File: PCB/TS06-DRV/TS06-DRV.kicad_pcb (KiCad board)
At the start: 2 copper layers, 100 x 70 mm, 38 parts, among them J1 TS06_JST_PH_S6B-PH-K-S_Back, U1 TS06_Arduino_Nano_Back, U11 TS06_DIP-8_Back, U12 TS06_DIP-8_Back, U13 TS06_PinHeader_1x05_Back, U14 TS06_R78E_SIP3_Back

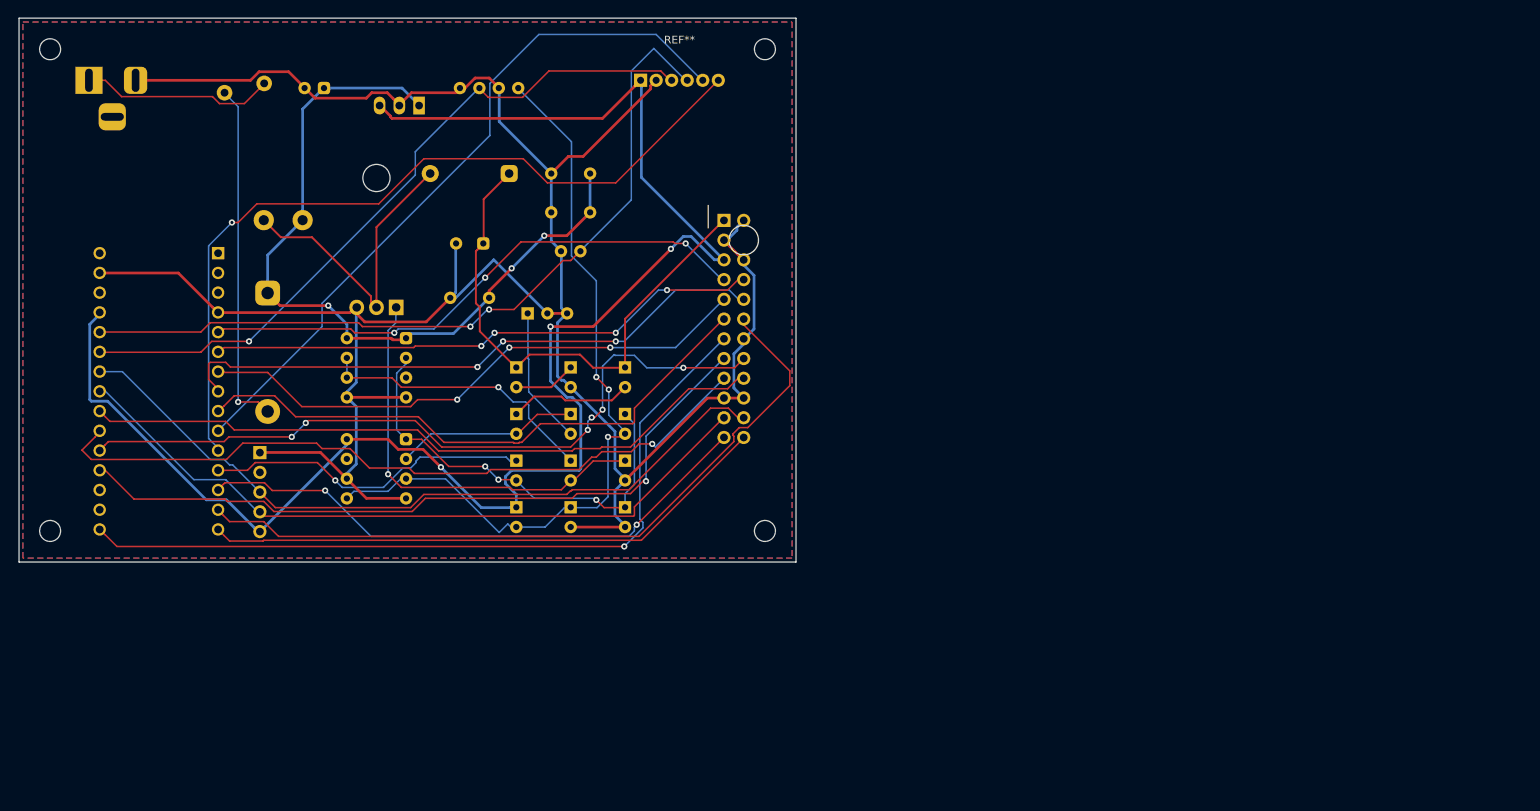
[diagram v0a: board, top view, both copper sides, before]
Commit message: TS06-DRV: routed, no vias, clean in KiCad 10's DRC
The route converged in negotiated routing: round 16, 0 nets sharing, 0 unrouted. A polish
pass then re-routed each net alone. The route is saved in tools/mkpcb_drv_routes.json, so the
board regenerates exactly.
- 1067 segments, 0 vias. Every strip pin and standoff lines up with TS06-DISP (check_mate()
  == []).
- checkcopper --hv is clean, audit.py is clean, and B.check finds 0 problems.
- KiCad 10 DRC: 0 errors and 0 unconnected. Four warnings remain:
  - the Nano's USB outline is proud of the edge, by design;
  - the stock silkscreen of VT21 and XS1 is clipped at their pads.

Fixes on the way:
- The router: an end snapped sideways onto another track now jogs to it instead of tilting
  the whole last run. A 13 mm GND run 0.1 mm out of true had clipped a U15 pad.
- The port-A bus and the LED ribbon are 0.24 mm wide. At their 0.45 mm pitch that leaves
  0.21 mm, not a rounding error under 0.2.
- Three GND pads whose back pour was a sliver fenced by tracks keep out of the pours. KiCad
  had reported starved thermals; the slivers now go as islands.
- References keep off every printed outline, the electrolytic's hatching included.
- audit.py measures a rotated text as rotated.
- plot() takes None as the default colour.

Co-Authored-By: Claude Opus 5.5 <noreply@anthropic.com>
Claude-Session: https://claude.ai/code/session_01WoV3gyAFgmtuk6W6Dr4bdA
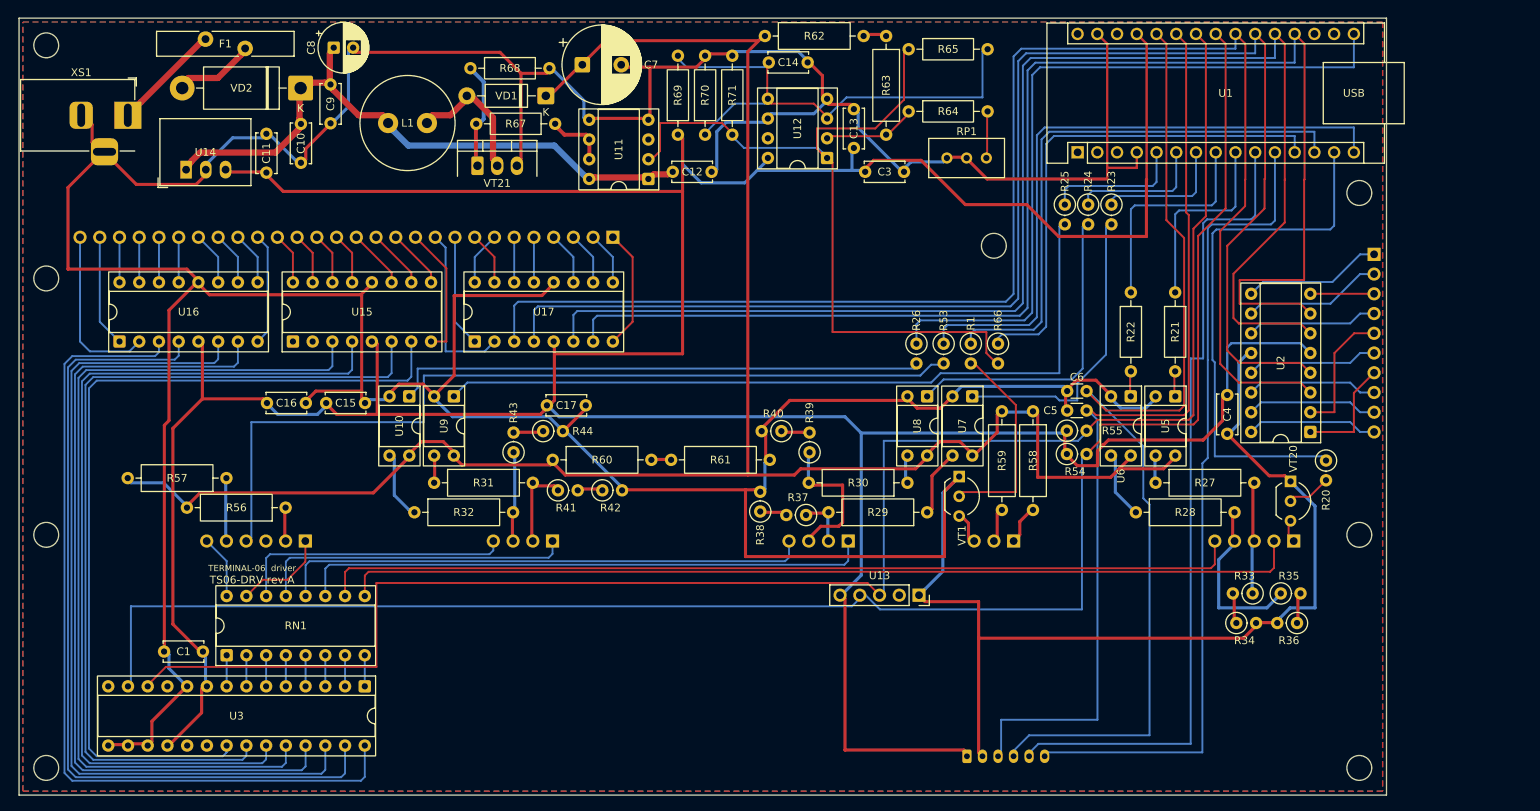
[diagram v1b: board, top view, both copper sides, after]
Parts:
- removed ? (x4): , MountingHole_2.7mm
- removed XJ2: TS06_PinHeader_2x12, TS06:TS06_PinHeader_2x12
- added C1: 100n, TS06:TS06_C_Disc_P5.00mm_R180, F.Cu at (23.7, 81.5)
- added C11: 10u, TS06:TS06_C_Disc_P5.00mm_R90, F.Cu at (31.8, 19.9)
- added C13: 100n, TS06:TS06_C_Disc_P5.00mm_R90, F.Cu at (107.4, 16.7)
- added C15: 100n, TS06:TS06_C_Disc_P5.00mm, F.Cu at (39.5, 49.5)
- added C16: 100n, TS06:TS06_C_Disc_P5.00mm, F.Cu at (31.9, 49.5)
- added C17: 100n, TS06:TS06_C_Disc_P5.00mm, F.Cu at (67.9, 49.8)
- added C3: 10u, TS06:TS06_C_Disc_P5.00mm, F.Cu at (108.9, 19.8)
- added C4: 100n, TS06:TS06_C_Disc_P5.00mm_R270, F.Cu at (155.5, 48.5)
- added H1: TS06_MountingHole_M3, TS06:TS06_MountingHole_M3, F.Cu at (172.5, 66.5)
- added H2: TS06_MountingHole_M3, TS06:TS06_MountingHole_M3, F.Cu at (3.50, 66.5)
- added H3: TS06_MountingHole_M3, TS06:TS06_MountingHole_M3, F.Cu at (125.5, 29.3)
- added H4: TS06_MountingHole_M3, TS06:TS06_MountingHole_M3, F.Cu at (3.50, 33.5)
- added H5: TS06_MountingHole_M3, TS06:TS06_MountingHole_M3, F.Cu at (3.50, 96.5)
- added H6: TS06_MountingHole_M3, TS06:TS06_MountingHole_M3, F.Cu at (172.5, 96.5)
- added H7: TS06_MountingHole_M3, TS06:TS06_MountingHole_M3, F.Cu at (3.50, 3.50)
- added H8: TS06_MountingHole_M3, TS06:TS06_MountingHole_M3, F.Cu at (172.5, 22.5)
- added R1: 10k, TS06:TS06_R_Axial_DIN0207_P2.54mm_Vertical_R270, F.Cu at (122.5, 41.9)
- added R20: 470R, TS06:TS06_R_Axial_DIN0207_P2.54mm_Vertical_R270, F.Cu at (168.2, 56.9)
- added R21: 470R, TS06:TS06_R_Axial_DIN0207_P10.16mm_R270, F.Cu at (148.8, 35.3)
- added R22: 470R, TS06:TS06_R_Axial_DIN0207_P10.16mm_R270, F.Cu at (143.1, 35.3)
- added R23: 470R, TS06:TS06_R_Axial_DIN0207_P2.54mm_Vertical_R270, F.Cu at (140.6, 24.0)
- added R24: 470R, TS06:TS06_R_Axial_DIN0207_P2.54mm_Vertical_R270, F.Cu at (137.6, 24.0)
- added R25: 470R, TS06:TS06_R_Axial_DIN0207_P2.54mm_Vertical_R270, F.Cu at (134.6, 24.0)
- added R26: 470R, TS06:TS06_R_Axial_DIN0207_P2.54mm_Vertical_R270, F.Cu at (115.5, 41.9)
- added R27: 6k8 TBC, TS06:TS06_R_Axial_DIN0309_P12.70mm, F.Cu at (146.3, 59.8)
- added R28: 6k8 TBC, TS06:TS06_R_Axial_DIN0309_P12.70mm, F.Cu at (143.7, 63.6)
- added R29: 6k8 TBC, TS06:TS06_R_Axial_DIN0309_P12.70mm_R180, F.Cu at (116.9, 63.6)
- added R30: 6k8 TBC, TS06:TS06_R_Axial_DIN0309_P12.70mm_R180, F.Cu at (114.3, 59.8)
- added R31: 12k, TS06:TS06_R_Axial_DIN0309_P12.70mm, F.Cu at (53.4, 59.8)
- added R32: 12k, TS06:TS06_R_Axial_DIN0309_P12.70mm, F.Cu at (50.9, 63.6)
- added R33: 510k DNP, TS06:TS06_R_Axial_DIN0207_P2.54mm_Vertical_R180, F.Cu at (158.8, 74.0)
- added R34: 510k DNP, TS06:TS06_R_Axial_DIN0207_P2.54mm_Vertical, F.Cu at (156.7, 77.8)
- added R35: 510k DNP, TS06:TS06_R_Axial_DIN0207_P2.54mm_Vertical, F.Cu at (162.4, 74.0)
- added R36: 510k DNP, TS06:TS06_R_Axial_DIN0207_P2.54mm_Vertical_R180, F.Cu at (164.5, 77.8)
- added R37: 510k DNP, TS06:TS06_R_Axial_DIN0207_P2.54mm_Vertical_R180, F.Cu at (101.3, 64.0)
- added R38: 510k DNP, TS06:TS06_R_Axial_DIN0207_P2.54mm_Vertical_R90, F.Cu at (95.4, 63.5)
- added R39: 510k DNP, TS06:TS06_R_Axial_DIN0207_P2.54mm_Vertical_R90, F.Cu at (101.7, 55.9)
- added R40: 510k DNP, TS06:TS06_R_Axial_DIN0207_P2.54mm_Vertical_R180, F.Cu at (98.1, 53.2)
- added R41: 510k DNP, TS06:TS06_R_Axial_DIN0207_P2.54mm_Vertical, F.Cu at (69.4, 60.8)
- added R42: 510k DNP, TS06:TS06_R_Axial_DIN0207_P2.54mm_Vertical, F.Cu at (75.1, 60.8)
- added R43: 510k DNP, TS06:TS06_R_Axial_DIN0207_P2.54mm_Vertical_R90, F.Cu at (63.6, 55.9)
- added R44: 510k DNP, TS06:TS06_R_Axial_DIN0207_P2.54mm_Vertical, F.Cu at (67.5, 53.2)
- added R53: 220R, TS06:TS06_R_Axial_DIN0207_P2.54mm_Vertical_R270, F.Cu at (119.0, 41.9)
- added R54: 4k7, TS06:TS06_R_Axial_DIN0207_P2.54mm_Vertical, F.Cu at (134.9, 56.1)
- added R55: 4k7, TS06:TS06_R_Axial_DIN0207_P2.54mm_Vertical, F.Cu at (134.9, 53.1)
- added R56: 8k2, TS06:TS06_R_Axial_DIN0309_P12.70mm_R180, F.Cu at (34.3, 63.0)
- added R57: 8k2, TS06:TS06_R_Axial_DIN0309_P12.70mm_R180, F.Cu at (26.7, 59.2)
- added R58: 220k, TS06:TS06_R_Axial_DIN0309_P12.70mm_R270, F.Cu at (130.5, 50.6)
- added R59: 220k, TS06:TS06_R_Axial_DIN0309_P12.70mm_R270, F.Cu at (126.5, 50.6)
- added RN1: 8x220R isolated DIP-16, TS06:TS06_DIP-16_W7.62mm_Socket_R90, F.Cu at (26.7, 82.0)
- added U10: TLP627, TS06:TS06_DIP-4_W7.62mm_Socket_R270, F.Cu at (50.2, 48.7)
- added U15: K155ID1, TS06:TS06_DIP-16_W7.62mm_Socket_R90, F.Cu at (35.2, 41.6)
- added U16: K155ID1, TS06:TS06_DIP-16_W7.62mm_Socket_R90, F.Cu at (12.9, 41.6)
- added U17: K155ID1, TS06:TS06_DIP-16_W7.62mm_Socket_R90, F.Cu at (58.6, 41.6)
- added U2: K155ID1, TS06:TS06_DIP-16_W7.62mm_Socket_R180, F.Cu at (166.2, 53.3)
- added U3: MCP23017-E/SP, TS06:TS06_DIP-28_W7.62mm_Socket_R270, F.Cu at (44.5, 86.0)
- added U5: TLP627, TS06:TS06_DIP-4_W7.62mm_Socket_R270, F.Cu at (148.8, 48.7)
- added U6: TLP627, TS06:TS06_DIP-4_W7.62mm_Socket_R270, F.Cu at (143.1, 48.7)
- added U7: TLP627, TS06:TS06_DIP-4_W7.62mm_Socket_R270, F.Cu at (122.7, 48.7)
- added U8: TLP627, TS06:TS06_DIP-4_W7.62mm_Socket_R270, F.Cu at (116.9, 48.7)
- added U9: TLP627, TS06:TS06_DIP-4_W7.62mm_Socket_R270, F.Cu at (56.0, 48.7)
- added VT1: MPSA42, TS06:TS06_TO-92_Inline_Wide_R270, F.Cu at (121.0, 59.0)
- added VT20: MPSA42, TS06:TS06_TO-92_Inline_Wide_R270, F.Cu at (163.6, 59.6)
- added XS11: PBS-10 female 2.54, TS06:TS06_PinSocket_1x10_R180, B.Cu at (174.4, 30.4)
- added XS12: PBS-28 female 2.54, TS06:TS06_PinSocket_1x28_R270, B.Cu at (76.4, 28.2)
- added XS21: PBS-5 female 2.54, TS06:TS06_PinSocket_1x05_R270, B.Cu at (164.1, 67.3)
- added XS22: PBS-3 female 2.54, TS06:TS06_PinSocket_1x03_R270, B.Cu at (128.0, 67.3)
- added XS23: PBS-4 female 2.54, TS06:TS06_PinSocket_1x04_R270, B.Cu at (106.7, 67.3)
- added XS24: PBS-4 female 2.54, TS06:TS06_PinSocket_1x04_R270, B.Cu at (68.7, 67.3)
- added XS25: PBS-6 female 2.54, TS06:TS06_PinSocket_1x06_R270, B.Cu at (36.9, 67.3)
- C10: value TS06_C_Disc_P5.00mm_Back -> 10u 25V; footprint TS06:TS06_C_Disc_P5.00mm_Back -> TS06:TS06_C_Disc_P5.00mm_R270; moved to F.Cu
- C12: value TS06_C_Disc_P5.00mm_Back -> 1u 50V; footprint TS06:TS06_C_Disc_P5.00mm_Back -> TS06:TS06_C_Disc_P5.00mm; moved to F.Cu
- C14: value TS06_C_Disc_P2.50mm_Back -> 100n; footprint TS06:TS06_C_Disc_P2.50mm_Back -> TS06:TS06_C_Disc_P5.00mm; moved to F.Cu
- C5, C6: value TS06_C_Disc_P2.50mm_Back -> 100n; footprint TS06:TS06_C_Disc_P2.50mm_Back -> TS06:TS06_C_Disc_P2.50mm_R180; moved to F.Cu
- C7: value TS06_CP_Radial_D8.0mm_P3.50mm_Back -> 4u7 400V; footprint TS06:TS06_CP_Radial_D8.0mm_P3.50mm_Back -> TS06:TS06_CP_Radial_D10.0mm_P5.00mm; moved to F.Cu
- C8: value TS06_CP_Radial_D6.3mm_P2.50mm_Back -> 100u 25V; footprint TS06:TS06_CP_Radial_D6.3mm_P2.50mm_Back -> TS06:TS06_CP_Radial_D6.3mm_P2.50mm; moved to F.Cu
- C9: value TS06_C_Disc_P5.00mm_Back -> 1u 50V; footprint TS06:TS06_C_Disc_P5.00mm_Back -> TS06:TS06_C_Disc_P5.00mm_R270; moved to F.Cu
- F1: value TS06_Fuse_Radial_MF-R_Back -> PTC 1.1A; footprint TS06:TS06_Fuse_Radial_MF-R_Back -> TS06:TS06_Fuse_PTC_MF-RG1100; moved to F.Cu
- J1: value TS06_JST_PH_S6B-PH-K-S_Back -> PH 6 vertical; footprint TS06:TS06_JST_PH_S6B-PH-K-S_Back -> TS06:TS06_JST_PH_B6B-PH-K_Vertical
- L1: value TS06_L_Radial_D10.0mm_P5.00mm_Back -> 220u 2A; footprint TS06:TS06_L_Radial_D10.0mm_P5.00mm_Back -> TS06:TS06_L_Radial_D12.0mm_P5.00mm; moved to F.Cu
- R60, R61: value TS06_R_Axial_L6.3mm_P2.54mm_Vertical_Back_R90 -> 470k; footprint TS06:TS06_R_Axial_L6.3mm_P2.54mm_Vertical_Back_R90 -> TS06:TS06_R_Axial_DIN0309_P12.70mm; moved to F.Cu
- R62: value TS06_R_Axial_L6.3mm_P2.54mm_Vertical_Back_R90 -> 750k 1%; footprint TS06:TS06_R_Axial_L6.3mm_P2.54mm_Vertical_Back_R90 -> TS06:TS06_R_Axial_DIN0309_P12.70mm; moved to F.Cu
- R63: value TS06_R_Axial_L6.3mm_P2.54mm_Vertical_Back_R90 -> 750k 1%; footprint TS06:TS06_R_Axial_L6.3mm_P2.54mm_Vertical_Back_R90 -> TS06:TS06_R_Axial_DIN0309_P12.70mm_R270; moved to F.Cu
- R64: value TS06_R_Axial_L6.3mm_P2.54mm_Vertical_Back_R90 -> 15k 1%; footprint TS06:TS06_R_Axial_L6.3mm_P2.54mm_Vertical_Back_R90 -> TS06:TS06_R_Axial_DIN0207_P10.16mm; moved to F.Cu
- R65: value TS06_R_Axial_L6.3mm_P2.54mm_Vertical_Back_R90 -> 1M; footprint TS06:TS06_R_Axial_L6.3mm_P2.54mm_Vertical_Back_R90 -> TS06:TS06_R_Axial_DIN0207_P10.16mm; moved to F.Cu
- R66: value TS06_R_Axial_L6.3mm_P2.54mm_Vertical_Back_R90 -> 2k2; footprint TS06:TS06_R_Axial_L6.3mm_P2.54mm_Vertical_Back_R90 -> TS06:TS06_R_Axial_DIN0207_P2.54mm_Vertical_R270; moved to F.Cu
- R67: value TS06_R_Axial_L6.3mm_P2.54mm_Vertical_Back_R90 -> 10R; footprint TS06:TS06_R_Axial_L6.3mm_P2.54mm_Vertical_Back_R90 -> TS06:TS06_R_Axial_DIN0207_P10.16mm_R180; moved to F.Cu
- R68: value TS06_R_Axial_L6.3mm_P2.54mm_Vertical_Back_R90 -> 10k; footprint TS06:TS06_R_Axial_L6.3mm_P2.54mm_Vertical_Back_R90 -> TS06:TS06_R_Axial_DIN0207_P10.16mm; moved to F.Cu
- R69, R70: value TS06_R_Axial_L6.3mm_P2.54mm_Vertical_Back_R90 -> 10k 1%; footprint TS06:TS06_R_Axial_L6.3mm_P2.54mm_Vertical_Back_R90 -> TS06:TS06_R_Axial_DIN0207_P10.16mm_R90; moved to F.Cu
- R71: value TS06_R_Axial_L6.3mm_P2.54mm_Vertical_Back_R90 -> 10k; footprint TS06:TS06_R_Axial_L6.3mm_P2.54mm_Vertical_Back_R90 -> TS06:TS06_R_Axial_DIN0207_P10.16mm_R90; moved to F.Cu
- RP1: value TS06_Trimmer_3296W_Back -> 10k; footprint TS06:TS06_Trimmer_3296W_Back -> TS06:TS06_Trimmer_3296W; moved to F.Cu
- U1: value TS06_Arduino_Nano_Back -> Arduino Nano; footprint TS06:TS06_Arduino_Nano_Back -> TS06:TS06_Arduino_Nano_R90; moved to F.Cu
- U11: value TS06_DIP-8_Back -> TC4420; footprint TS06:TS06_DIP-8_Back -> TS06:TS06_DIP-8_W7.62mm_Socket_R180; moved to F.Cu
- U12: value TS06_DIP-8_Back -> LM393; footprint TS06:TS06_DIP-8_Back -> TS06:TS06_DIP-8_W7.62mm_Socket_R180; moved to F.Cu
- U13: value TS06_PinHeader_1x05_Back -> DS3231 mini; footprint TS06:TS06_PinHeader_1x05_Back -> TS06:TS06_PinSocket_1x05_R270; moved to F.Cu
- U14: value TS06_R78E_SIP3_Back -> R-78E5.0-1.0; footprint TS06:TS06_R78E_SIP3_Back -> TS06:TS06_R-78E_SIP3; moved to F.Cu
- VD1: value TS06_D_DO-41_P10.16mm_Back -> HER106 / UF4007; footprint TS06:TS06_D_DO-41_P10.16mm_Back -> TS06:TS06_D_DO-41_P10.16mm_R180; moved to F.Cu
- VD2: value TS06_D_DO-201_P15.24mm_Back_R90 -> 1N5822; footprint TS06:TS06_D_DO-201_P15.24mm_Back_R90 -> TS06:TS06_D_DO-201AD_P15.24mm_R180; moved to F.Cu
- VT21: value TS06_TO-220_Horizontal_Back -> IRF840; footprint TS06:TS06_TO-220_Horizontal_Back -> TS06:TS06_TO-220-3_Vertical_HV; moved to F.Cu
- XS1: value TS06_BarrelJack_Back -> DC 5.5x2.1; footprint TS06:TS06_BarrelJack_Back -> TS06:TS06_BarrelJack_Horizontal; moved to F.Cu
- moved U1 122.2 mm to (136.2, 17.3)
- moved J1 94.5 mm to (122.0, 95.0)
- moved C5 89.6 mm to (137.4, 50.5)
- moved U13 85.9 mm to (115.8, 74.3)
- moved U12 70.5 mm to (104.0, 18.0)
- moved R63 69.0 mm to (111.6, 2.30)
- moved C6 68.8 mm to (137.4, 48.0)
- moved R66 64.1 mm to (126.0, 41.9)
- moved R65 60.5 mm to (114.5, 4.00)
- moved RP1 59.9 mm to (124.5, 18.0)
- moved R64 59.2 mm to (114.5, 12.0)
- moved R68 55.5 mm to (58.1, 6.45)
- moved R69 53.4 mm to (84.8, 15.0)
- moved R70 52.2 mm to (88.3, 15.0)
- moved R71 51.1 mm to (91.8, 15.0)
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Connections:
- XS1 pad 3: (no net) -> GND
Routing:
- net GND: track 320.2 -> 726.4 mm
- net +5V: track 210.1 -> 506.5 mm, vias 3 -> 0
- net HV185: track 68.6 -> 249.0 mm
- net SDA: track 92.9 -> 223.7 mm
- net BL_A1: track 0.00 -> 123.5 mm
- net SCL: track 96.0 -> 218.4 mm
- net BL_A2: track 0.00 -> 118.4 mm
- net XA3: track 0.00 -> 115.1 mm
- net XA1: track 0.00 -> 114.0 mm
- net XA2: track 0.00 -> 113.3 mm
- net XA0: track 0.00 -> 112.2 mm
- net M_A: track 0.00 -> 111.4 mm
- net XA7: track 0.00 -> 110.1 mm
- net XA5: track 0.00 -> 109.1 mm
- net XA6: track 0.00 -> 108.3 mm
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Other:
- board size 100 x 70 mm -> 176 x 100 mm
- board text added: "TERMINAL-06 driver"
- board text added: "TS06-DRV rev A"
- board text removed: "TS06-DRV TERMINAL-06"
- board text removed: "USB"

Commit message: TS06-DRV: re-routed on the widened 191.4 mm board; both boards re-verified
The route converged in negotiated routing at round 15, with 0 nets sharing and 0 unrouted. A
polish pass followed. The route is saved in tools/mkpcb_drv_routes.json.
- TS06-DRV:
  - 1097 segments (369 hand-laid), 0 vias; check_mate() == [];
  - checkcopper --hv clean, audit.py clean;
  - KiCad 10 DRC: 0 errors, 0 unconnected. Four warnings as before: the Nano's USB outline past
    the edge, and the stock silk of VT21 and XS1 clipped at their pads.
  - 5936 mm of signal copper, 1.33x its 4479 mm floor, 86.1 % square.
  - Three more ground pads, where the new route left back-face slivers, keep out of the pours.
- TS06-DISP: 0 vias; checkcopper --hv clean, audit.py clean; KiCad DRC 0 unconnected, with only
  the known colon overlaps.
- The case model re-renders: 204.4 x 120.3 x 83.6 mm. Its ИН-17 check reads 0.5 mm stem to
  stem, and 2.2 mm to the glass either side.
- BOMs: the XP12/XS12 strips are 31-pin.
- README: the width and why, and 'Checked' refreshed.
- The review: the ИН-17 finding is marked fixed. The swap layout is scored and recorded as the
  strongest alternative, not adopted. The fascia under a wider row is an open choice.

Co-Authored-By: Claude Opus 5.5 <noreply@anthropic.com>
Claude-Session: https://claude.ai/code/session_01WoV3gyAFgmtuk6W6Dr4bdA
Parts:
- R38, R39: footprint TS06:TS06_R_Axial_DIN0207_P2.54mm_Vertical_R90 -> TS06:TS06_R_Axial_DIN0207_P2.54mm_Vertical_R180
- R40: footprint TS06:TS06_R_Axial_DIN0207_P2.54mm_Vertical_R180 -> TS06:TS06_R_Axial_DIN0207_P2.54mm_Vertical_R90
- XS12: value PBS-28 female 2.54 -> PBS-31 female 2.54; footprint TS06:TS06_PinSocket_1x28_R270 -> TS06:TS06_PinSocket_1x31_R270
- moved R38 15.4 mm to (110.8, 63.3)
- moved C4 15.4 mm to (170.9, 48.5)
- moved C5 15.4 mm to (152.8, 50.5)
- moved C6 15.4 mm to (152.8, 48.0)
- moved H1 15.4 mm to (187.9, 66.5)
- moved H3 15.4 mm to (140.9, 29.3)
- moved H6 15.4 mm to (187.9, 96.5)
- moved H8 15.4 mm to (187.9, 22.5)
- moved J1 15.4 mm to (137.4, 95.0)
- moved R1 15.4 mm to (137.9, 41.9)
- moved R20 15.4 mm to (183.6, 56.9)
- moved R22 15.4 mm to (158.5, 35.3)
- moved R23 15.4 mm to (156.0, 24.0)
- moved R24 15.4 mm to (153.0, 24.0)
- moved R25 15.4 mm to (150.0, 24.0)
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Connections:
- XS12 pad 11: CAT_B_AMP -> (no net)
- XS12 pad 12: CAT_B_OHM -> (no net)
- XS12 pad 13: CAT_B_SIEMENS -> (no net)
- XS12 pad 14: CAT_B_VOLT -> CAT_B_AMP
- XS12 pad 15: CAT_B_HENRY -> CAT_B_OHM
- XS12 pad 16: CAT_B_HERTZ -> CAT_B_SIEMENS
- XS12 pad 17: CAT_B_FARAD -> CAT_B_VOLT
- XS12 pad 18: CAT_B_WATT -> CAT_B_HENRY
- XS12 pad 19: CAT_A_NANO -> CAT_B_HERTZ
- XS12 pad 20: CAT_A_PCT -> CAT_B_FARAD
- XS12 pad 21: CAT_A_PI -> CAT_B_WATT
- XS12 pad 22: CAT_A_KILO -> CAT_A_NANO
- XS12 pad 23: CAT_A_MEGA -> CAT_A_PCT
- XS12 pad 24: CAT_A_MILLI -> CAT_A_PI
- XS12 pad 25: CAT_A_PLUS -> CAT_A_KILO
- XS12 pad 26: CAT_A_MINUS -> CAT_A_MEGA
- XS12 pad 27: CAT_A_P -> CAT_A_MILLI
- XS12 pad 28: CAT_A_MICRO -> CAT_A_PLUS
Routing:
- net +5V: track 506.5 -> 598.8 mm
- net M_A: track 111.4 -> 145.1 mm
- net A6: track 120.5 -> 144.4 mm
- net HV185: track 249.0 -> 267.5 mm
- net BL_A4: track 68.7 -> 84.1 mm
- net BL_A3: track 73.8 -> 89.2 mm
- net BL_A2: track 118.4 -> 133.8 mm
- net BL_A1: track 123.5 -> 138.9 mm
- net SDA: track 223.7 -> 238.5 mm
- net PWM_G: track 100.2 -> 115.0 mm
- net SCL: track 218.4 -> 232.5 mm
- net A1: track 179.0 -> 190.6 mm
- net A7: track 129.9 -> 121.5 mm
- net OPT_S10: track 98.8 -> 106.6 mm
- net A2: track 186.2 -> 194.0 mm
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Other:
- board size 176 x 100 mm -> 191.4 x 100 mm

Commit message: TS06-DRV values and firmware soft-start: fixes from the electrical grill
- R56/R57, the static ИН-15 anode resistors: 8k2 -> 18k. The ИН-15s are
  lit continuously, so 8k2 ran them at 4.2-5.4 mA, about twice the
  rated 2.5 mA. 18k gives 2.5 mA at a 140 V sustaining voltage.
- R64 15k -> 18k and RP1 10k -> 5k: the set point now spans 165-210 V
  and reaches 185 V near mid-travel. At one end of the old trimmer it
  reached 252 V.
- Firmware: the HV PWM ramps from 20 to DUTY over about 85 ms. Jumping
  straight to DUTY with C7 at 12 V let L1's current ratchet past
  saturation for 15-20 ms. Types 0 and 4 compile.

The board changed in its value fields only. KiCad 10 DRC: 0 errors,
0 unconnected, the same 4 accepted warnings. checkcopper --hv and audit
are clean, and check_mate() == [].

Co-Authored-By: Claude Opus 5.5 <noreply@anthropic.com>
Claude-Session: https://claude.ai/code/session_01WoV3gyAFgmtuk6W6Dr4bdA
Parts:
- R56, R57: value 8k2 -> 18k
- R64: value 15k 1% -> 18k 1%
- RP1: value 10k -> 5k
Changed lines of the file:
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@@
 			)
 		)
-		(property "Value" "8k2"
+		(property "Value" "18k"
 			(at -6.35 -2.72 0)
 			(layer "F.Fab")
@@
 			)
 		)
-		(property "Value" "8k2"
+		(property "Value" "18k"
 			(at -6.35 -2.72 0)
 			(layer "F.Fab")
@@
 			)
 		)
-		(property "Value" "15k 1%"
+		(property "Value" "18k 1%"
 			(at 5.08 2.37 0)
 			(layer "F.Fab")
@@
 			)
 		)
-		(property "Value" "10k"
+		(property "Value" "5k"
 			(at -2.54 3.67 0)
 			(layer "F.Fab")
